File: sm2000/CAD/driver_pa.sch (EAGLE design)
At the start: 31 parts, among them Q1 BRF92, Q2 BFQ19, Q3 BFQ19, U1 PGA-103+, X1 BU-SMA-G, X2 BU-SMA-G

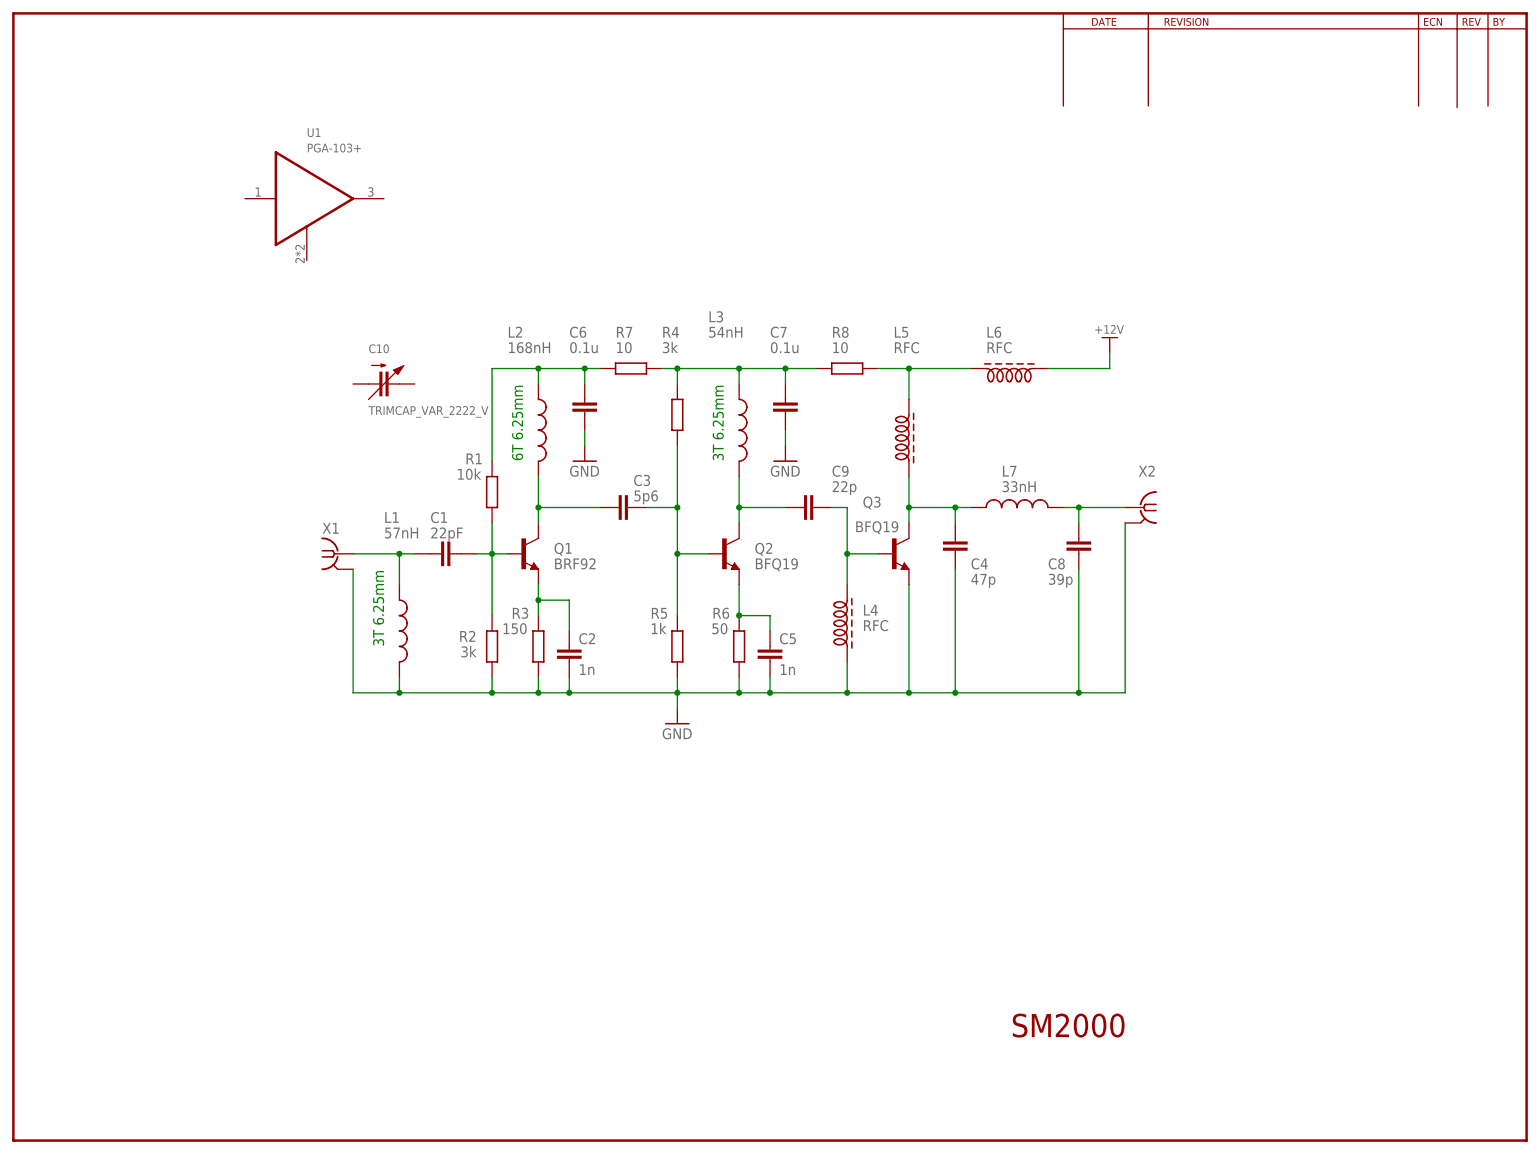
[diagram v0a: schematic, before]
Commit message: rename test to driver_pa, updated PA with RSD01MUS2 and 5th order cheby filter
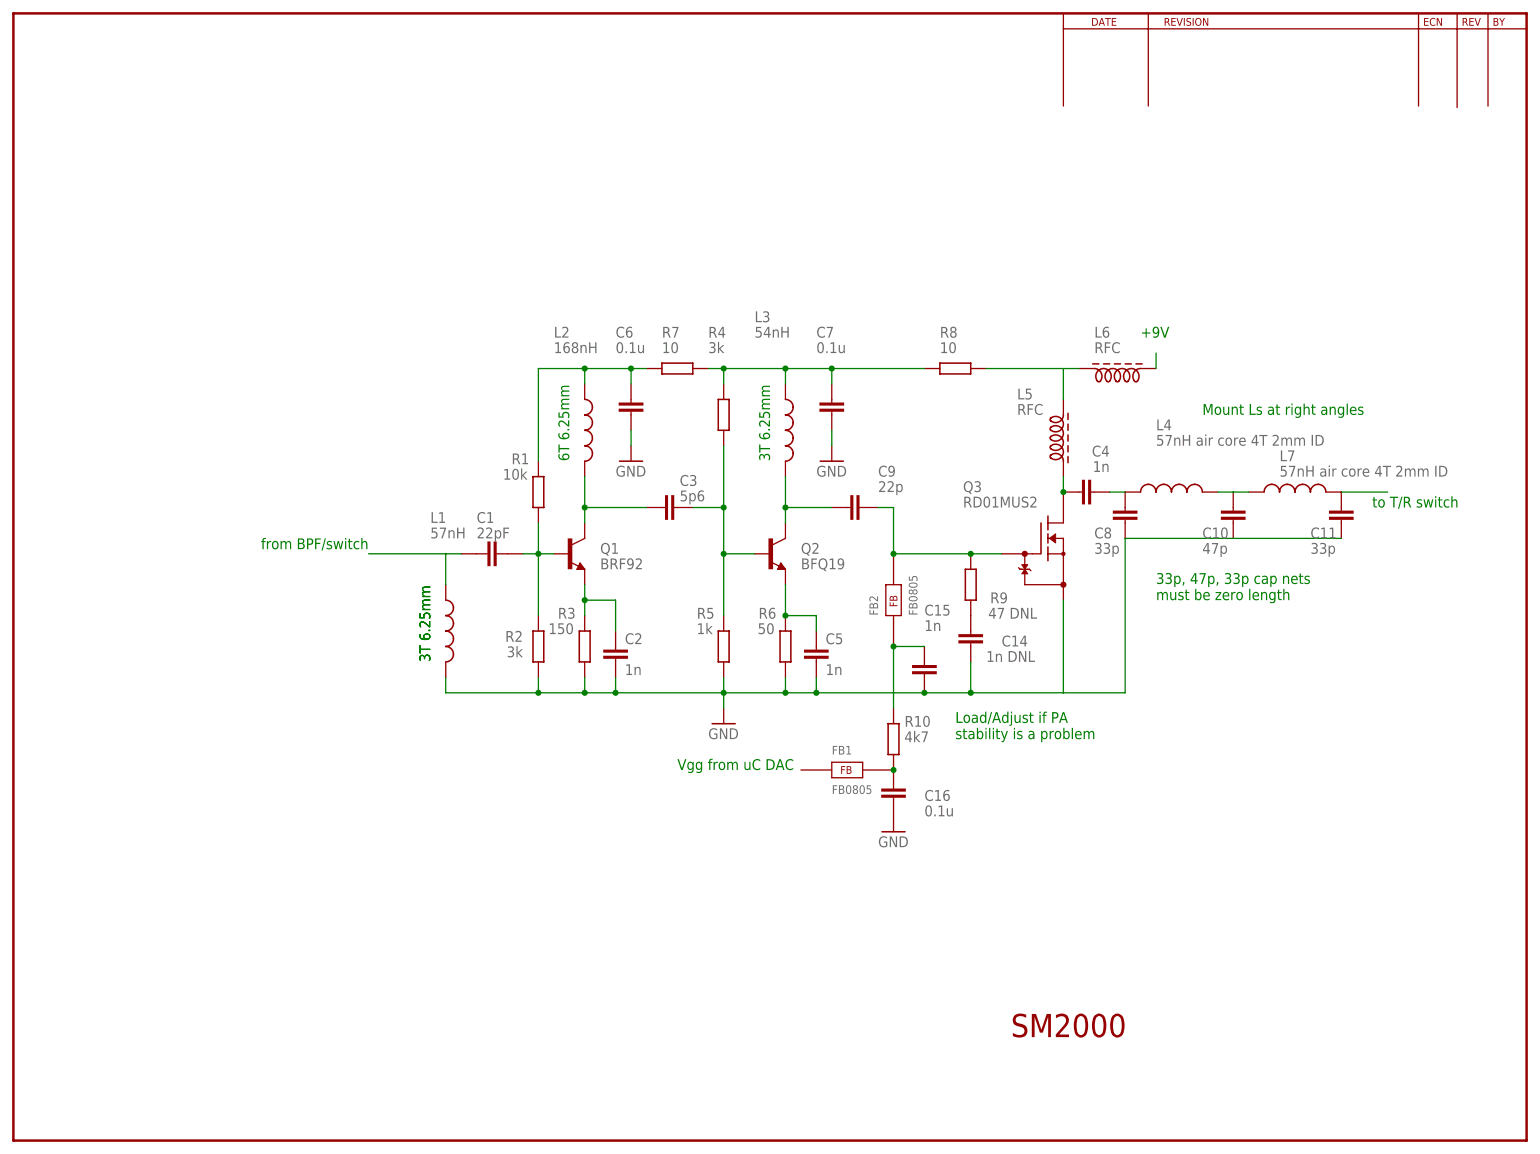
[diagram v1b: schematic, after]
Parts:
- removed U1: PGA-103+, _RoweTel:PGA-103+
- removed X1, X2: BU-SMA-G, con-coax:BU-SMA-G
- added C11: 33p, rcl:C-EU025-024X044
- added C14: 1n DNL, rcl:C-EU025-024X044
- added C15: 1n, rcl:C-EU025-024X044
- added C16: 0.1u, rcl:C-EU025-024X044
- added FB1, FB2: FB0805, _RoweTel:FB0805
- added R10: 4k7, AA-ipc-7351-resistor:RESISTOR_0805
- added R9: 47 DNL, AA-ipc-7351-resistor:RESISTOR_0805
- C10: value TRIMCAP_VAR_2222_V -> 47p; device _RoweTel:TRIMCAP_VAR_2222_V -> rcl:C-EU025-024X044
- C4: value 47p -> 1n
- C8: value 39p -> 33p
- L4: value RFC -> 57nH air core 4T 2mm ID; device inductor-neosid:Z14/40CCW -> rcl:L-US0204/5
- L7: value 33nH -> 57nH air core 4T 2mm ID
- Q3: value BFQ19 -> RD01MUS2; device transistor:-NPN-SOT23-EBC -> _RoweTel:RD01MUS2
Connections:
- net +12V renamed N$19
- new net N$17: C1.2, L1.1
- new net N$18: C16.1, FB1.2, R10.1
- new net N$20: C4.1, L5.1, Q3.D
- new net N$7: C4.2, C8.1, L4.1
- new net N$8: C10.1, L4.2, L7.1
- net GND: now also C11.2, C14.2, C15.2, C16.2, Q3.S; no longer C4.2, L4.1, Q3.E, X1.2, X2.2
- net N$12: now also C11.1, L7.2; no longer C4.1, L5.1, L7.1, Q3.C
- net N$15: now also FB2.2, Q3.G, R9.2; no longer L4.2, Q3.B
- net N$2: now also C14.1, R9.1; no longer C1.2, L1.1, X1.1
- net N$5: now also C15.1, FB2.1, R10.2; no longer C8.1, L7.2, X2.1
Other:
- note added: "+9V"
- note added: "33p, 47p, 33p cap nets must be zero length"
- note added: "Load/Adjust if PA stability is a problem"
- note added: "Mount Ls at right angles"
- note added: "Vgg from uC DAC"
- note added: "from BPF/switch"
- note added: "to T/R switch"
- moved on the sheet: C1, C2, C3, C4, C5, C6, C7, C8, C9, L1, L2, L3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
